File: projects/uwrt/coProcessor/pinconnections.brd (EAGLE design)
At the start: 101.6 x 101.6 mm, 26 parts, among them U1 MPU-9250, U3 HTU21D

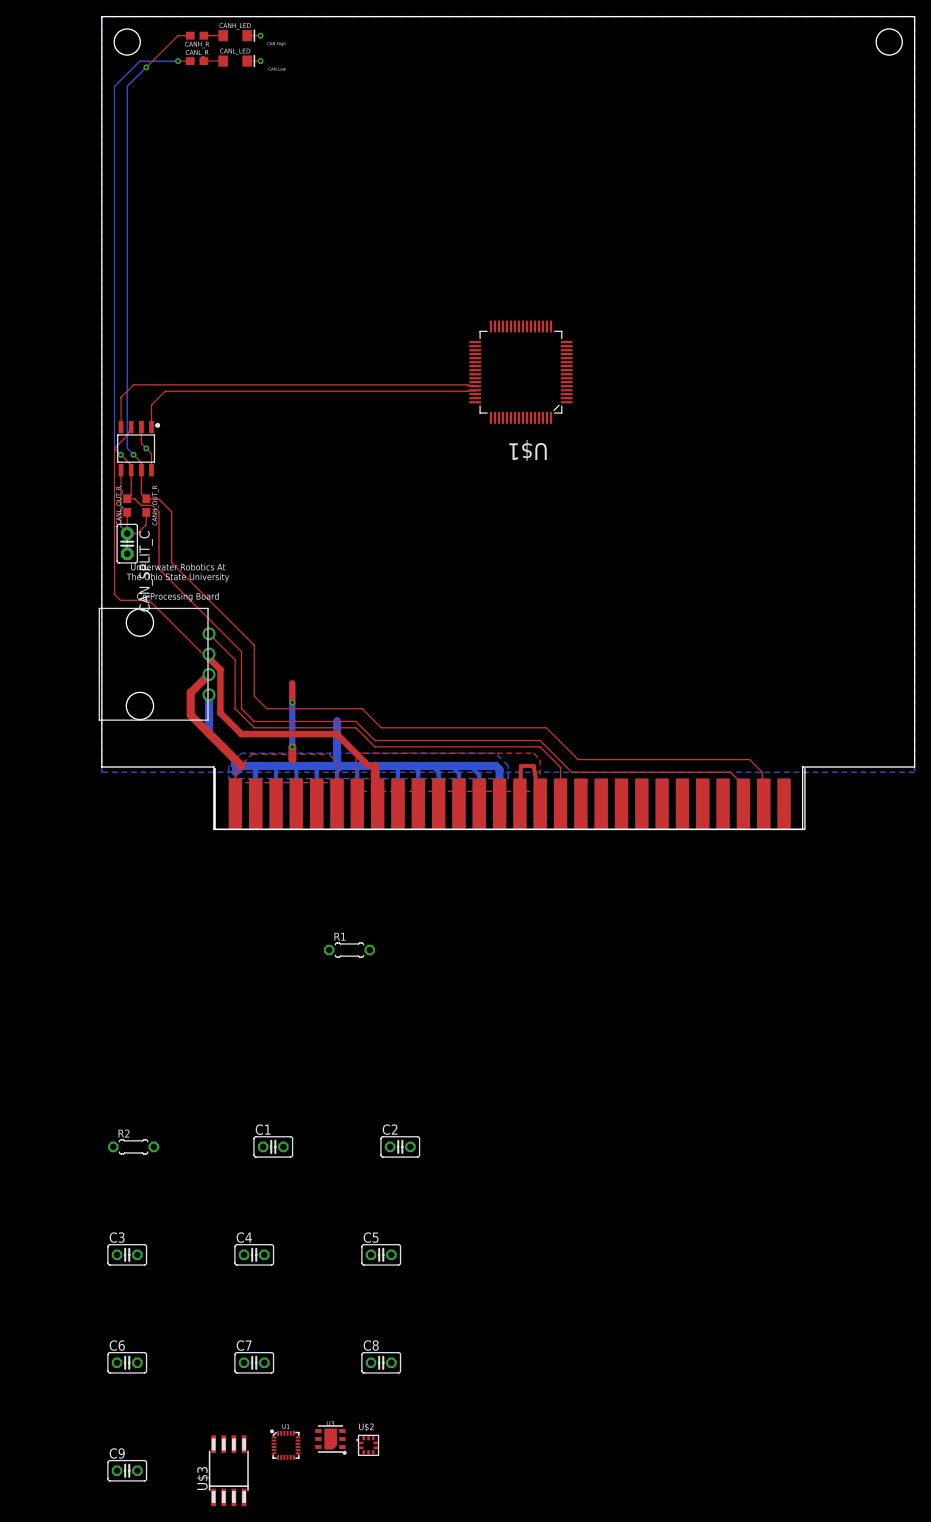
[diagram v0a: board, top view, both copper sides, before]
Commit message: Merged template with coPro connections
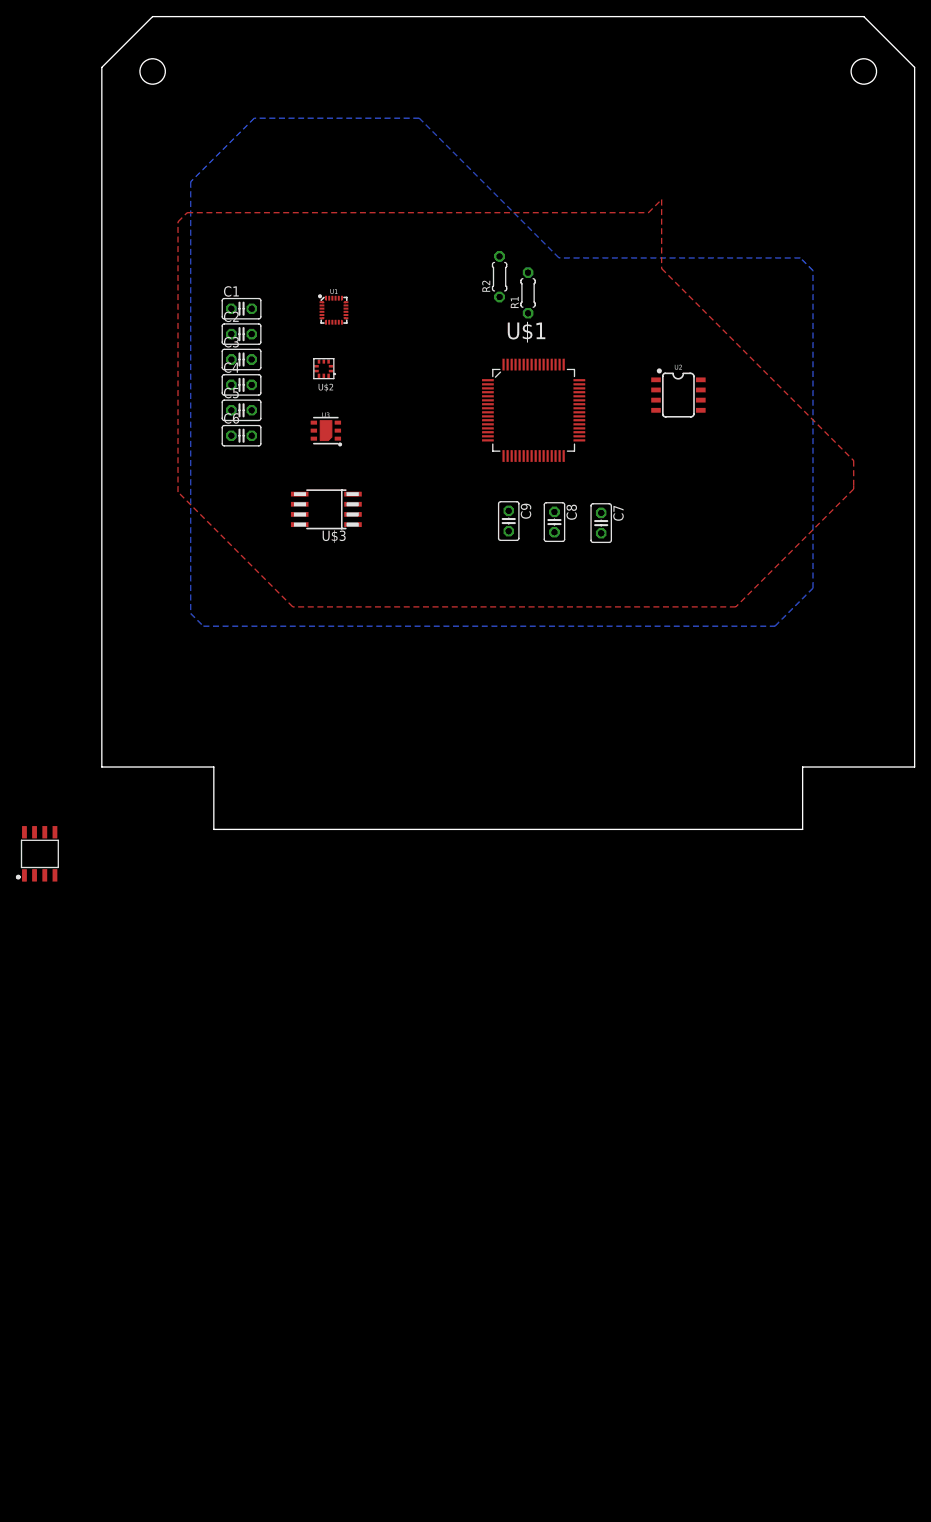
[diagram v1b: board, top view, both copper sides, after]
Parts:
- removed CANH_LED, CANL_LED: (no value), SparkFun-LED:LED-1206
- removed CANH_OUT_R, CANL_OUT_R: 60, SparkFun-Resistors:0603
- removed CANH_R, CANL_R: 330, SparkFun-Resistors:0603
- removed CAN_SPLIT_C: 4700pF, capacitor-wima:C2.5-2
- removed MCP2561: MCP2561, MCP2561:SOIC8
- removed U$7: 70555-0003, molex:70555-0003
- added U2: MCP2551, SparkFun-IC-Comms:SO08
- U$4: value 5530843-6-STS -> MCP2561; device te-connectivity:5530843-6-BOARD -> MCP2561:SOIC8
- moved U1 142.0 mm to (29.0, 64.9)
- moved U$2 134.7 mm to (27.7, 57.6), turned to 180 degrees
- moved C9 127.9 mm to (50.9, 38.5), turned to 270 degrees
- moved U3 126.0 mm to (28.0, 49.8)
- moved U$3 120.8 mm to (28.1, 40.0), turned to 90 degrees
- moved R2 118.0 mm to (49.7, 69.1), turned to 90 degrees
- moved C6 116.8 mm to (17.5, 49.2)
- moved C7 113.6 mm to (62.4, 38.3), turned to 270 degrees
- moved C3 112.8 mm to (17.5, 58.7)
- moved C4 108.8 mm to (17.5, 55.6)
- moved C8 107.3 mm to (56.6, 38.4), turned to 270 degrees
- moved C5 107.0 mm to (17.5, 52.4)
- moved C1 104.9 mm to (17.5, 65.1)
- moved C2 103.5 mm to (17.5, 61.9)
- moved R1 85.1 mm to (53.3, 67.1), turned to 90 degrees
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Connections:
- removed net +5V: MCP2561.P$3, U$4.13, U$4.15, U$4.17, U$4.19, U$4.21, U$4.23, U$4.25, U$4.27, U$4.29, U$4.31, U$7.3
- removed net 12V_OUT: U$4.33, U$7.4
- removed net CANH_LED: CANH_LED.A, CANH_R.1
- removed net CANH_OUT: CANH_OUT_R.1, CANH_R.2, MCP2561.P$7, U$4.53
- removed net CANL_LED: CANL_LED.A, CANL_R.2
- removed net CANL_OUT: CANL_OUT_R.2, CANL_R.1, MCP2561.P$6, U$4.51
- removed net CAN_RX: MCP2561.P$4, U$1.44
- removed net CAN_SPLIT: CANH_OUT_R.2, CANL_OUT_R.1, CAN_SPLIT_C.1, MCP2561.P$5
- removed net CAN_TX: MCP2561.P$1, U$1.45
- removed net N$15: U$4.35
- removed net N$2 (its old number): R2.1, U$1.59
- new net N$5: U$1.44, U2.4
- new net N$6: U2.6
- new net N$7: U2.7
- new net SCL: R1.1, U$1.58, U$2.2, U$3.6, U1.23, U3.SCK
- new net SDA: R2.1, U$1.59, U$2.4, U$3.5, U1.24, U3.DATA
- new net VDD: C2.1, C3.1, C4.1, C5.1, C6.1, C9.1, R1.2, R2.2, U$1.13, U$1.19, U$1.64, U$2.1, U$2.10, U$2.5, U$2.6, U$3.8, U1.1, U1.13, U1.22, U1.8, U1.9, U2.3, U3.VDD
- net +3V3: no longer C2.1, C3.1, C4.1, C5.1, C6.1, C9.1, R1.2, R2.2, U$1.13, U$1.19, U$1.64, U$2.1, U$2.10, U$4.1, U$4.11, U$4.3, U$4.5, U$4.7, U$4.9, U$7.2, U1.1, U1.13, U1.8, U3.VDD
- net GND: now also U$3.7, U2.2; no longer CANH_LED.C, CANL_LED.C, CAN_SPLIT_C.2, MCP2561.P$2, MCP2561.P$8, U$4.10, U$4.12, U$4.14, U$4.16, U$4.18, U$4.2, U$4.20, U$4.22, U$4.24, U$4.26, U$4.28, U$4.4, U$4.6, U$4.8, U$7.1
- net N$3: now also U$1.45, U2.1; no longer R1.1, U$1.58
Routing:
- net CANL_OUT: track 166.0 -> 0.00 mm, vias 2 -> 0
- net CANH_OUT: track 164.8 -> 0.00 mm, vias 2 -> 0
- net GND: track 132.5 -> 0.00 mm, vias 3 -> 0
- net +5V: track 82.3 -> 0.00 mm
- net 12V_OUT: track 59.0 -> 0.00 mm
- net CAN_RX: track 48.7 -> 0.00 mm
- net CAN_TX: track 44.0 -> 0.00 mm
- net +3V3: track 29.6 -> 0.00 mm, vias 2 -> 0
- net CAN_SPLIT: track 15.2 -> 0.00 mm
- net CANL_LED: track 2.41 -> 0.00 mm
- net CANH_LED: track 2.41 -> 0.00 mm
- added copper zone on layer 1, net VDD
- removed copper zone on layer 1, net +3V3
- removed copper zone on layer 1, net +5V
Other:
- outline, holes or cut-outs redrawn
- board text removed: "CAN High"
- board text removed: "CAN Low"
- board text removed: "Underwater Robotics At The Ohio State University Co-Processing Board"
